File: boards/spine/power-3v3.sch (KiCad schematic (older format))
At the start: 14 parts, among them U9 RT8299A

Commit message: BOM tweaks, starting DC/DC fixes
VCC is not active until EN goes high, so EN must be
connected to VIN via the 100k resistor. Internal resistance
is 5k to a 3V zener.
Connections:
- net +5V: now also R25.1
- net at C57.1, U9.8 (VCC): no longer R25.1
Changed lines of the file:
@@
 	4250 4300 4150 4300
-Wire Wire Line
-	4150 4300 4150 4050
-Connection ~ 4150 4050
 Wire Wire Line
 	6250 3800 6500 3800
@@
 Text Notes 3750 5100 0    60   ~ 0
 High efficiency DC-DC converter, 3.3V at 3A
+Wire Wire Line
+	4150 4300 4150 3800
+Connection ~ 4150 3800
 $EndSCHEMATC

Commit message: BOM cleanup
Especially fix the confusing and mostly incorrect Mfg/Mfr stuff that I inherited from somewhere.
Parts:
- C55, C56, C60, C61: Mfg1 (none) -> Murata; Mfg1Id (none) -> GRM31CR61H106MA12L; MfgId GRM31CR61H106MA12L -> (none); MfrId Murata -> (none)
- C57: Mfg1 (none) -> Murata; Mfg1Id (none) -> GRM219R61H105KA73D; MfgId GRM219R61H105KA73D -> (none); MfrId Murata -> (none)
- C58: Mfg1 (none) -> Murata; Mfg1Id (none) -> GRM21BR71H104MA01L; MfgId GRM21BR71H104MA01L -> (none); MfrId Murata -> (none)
- C59: Mfg1 (none) -> Murata; Mfg1Id (none) -> GRM2165C1H101JA01D; MfgId GRM2165C1H101JA01D -> (none); MfrId Murata -> (none)
- D6: Mfg1 (none) -> Diodes Inc; Mfg1Id (none) -> BAT54C-7-F; MfgId BAT54C-7-F -> (none); MfrId Diodes Inc -> (none)
- L2: Mfg1 (none) -> Bourns; Mfg1Id (none) -> SRR1280-220M; MfgId Bourns -> (none); MfrId SRR1280-220M -> (none)
- R25: Mfg1 (none) -> Stackpole; Mfg1Id (none) -> RMCF0805JT100K; MfgId RMCF0805JT100K -> (none); MfrId Stackpole -> (none)
- R26: Mfg1 (none) -> Stackpole; Mfg1Id (none) -> RMCF0805JT150R; MfgId RMCF0805JT150R -> (none); MfrId Stackpole -> (none)
- R27: Mfg1 (none) -> Stackpole; Mfg1Id (none) -> RMCF0805FT16K0; MfgId RMCF0805FT16K0 -> (none); MfrId Stackpole -> (none)
- R28: Mfg1 (none) -> Stackpole; Mfg1Id (none) -> RMCF0805FT5K10; MfgId RMCF0805FT5K10 -> (none); MfrId Stackpole -> (none)
- U9: Mfg1 (none) -> Richtek; Mfg1Id (none) -> RT8299AZSP; MfgId RT8299AZSP -> (none); MfrId Richtek -> (none)
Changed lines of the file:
@@
 F 3 "https://www.seielect.com/Catalog/SEI-RMCF_RMCP.pdf" H 4400 4300 30  0001 C CNN
 F 4 "Digikey" V 4400 4300 60  0001 C CNN "Vend1"
-F 5 "Stackpole" V 4400 4300 60  0001 C CNN "MfrId"
-F 6 "RMCF0805JT100K" V 4400 4300 60  0001 C CNN "MfgId"
+F 5 "Stackpole" V 4400 4300 60  0001 C CNN "Mfg1"
+F 6 "RMCF0805JT100K" V 4400 4300 60  0001 C CNN "Mfg1Id"
 F 7 "RMCF0805JT100KCT-ND" V 4400 4300 60  0001 C CNN "Vend1Id"
 F 8 "0.00320" V 4400 4300 60  0001 C CNN "RefPrice1k"
@@
 F 2 "Capacitors_SMD:C_1206" H 3338 4050 30  0001 C CNN
 F 3 "http://www.murata.com/~/media/webrenewal/support/library/catalog/products/capacitor/mlcc/c02e.ashx" H 3300 4200 60  0001 C CNN
-F 4 "GRM31CR61H106MA12L" H 3350 4000 39  0001 L BNN "MfgId"
-F 5 "Murata" H 3300 4200 60  0001 C CNN "MfrId"
+F 4 "GRM31CR61H106MA12L" H 3350 4000 39  0001 L BNN "Mfg1Id"
+F 5 "Murata" H 3300 4200 60  0001 C CNN "Mfg1"
 F 6 "Digikey" H 3300 4200 60  0001 C CNN "Vend1"
 F 7 "490-10756-2-ND" H 3300 4200 60  0001 C CNN "Vend1Id"
@@
 F 2 "Capacitors_SMD:C_0805" H 3888 4200 30  0001 C CNN
 F 3 "http://www.murata.com/~/media/webrenewal/support/library/catalog/products/capacitor/mlcc/c02e.ashx" H 3850 4350 60  0001 C CNN
-F 4 "GRM219R61H105KA73D" H 3900 4150 39  0001 L BNN "MfgId"
-F 5 "Murata" H 3850 4350 60  0001 C CNN "MfrId"
+F 4 "GRM219R61H105KA73D" H 3900 4150 39  0001 L BNN "Mfg1Id"
+F 5 "Murata" H 3850 4350 60  0001 C CNN "Mfg1"
 F 6 "Digikey" H 3850 4350 60  0001 C CNN "Vend1"
 F 7 "490-10743-2-ND" H 3850 4350 60  0001 C CNN "Vend1Id"
@@
 F 4 "Digikey" H 5050 3600 60  0001 C CNN "Vend1"
 F 5 "1028-1295-1-ND" H 5050 3600 60  0001 C CNN "Vend1Id"
-F 6 "Richtek" H 5050 3600 60  0001 C CNN "MfrId"
-F 7 "RT8299AZSP" H 5050 3600 60  0001 C CNN "MfgId"
+F 6 "Richtek" H 5050 3600 60  0001 C CNN "Mfg1"
+F 7 "RT8299AZSP" H 5050 3600 60  0001 C CNN "Mfg1Id"
 F 8 "0.37752" H 5050 3600 60  0001 C CNN "RefPrice1k"
 	1    5050 3600
@@
 F 5 "490-9672-2-ND" V 6100 3800 60  0001 C CNN "Vend1Id"
 F 6 "Digikey" V 6100 3800 60  0001 C CNN "Vend1"
-F 7 "Murata" V 6100 3800 60  0001 C CNN "MfrId"
-F 8 "GRM21BR71H104MA01L" V 6100 3800 60  0001 C CNN "MfgId"
+F 7 "Murata" V 6100 3800 60  0001 C CNN "Mfg1"
+F 8 "GRM21BR71H104MA01L" V 6100 3800 60  0001 C CNN "Mfg1Id"
 	1    6100 3800
 	0    1    1    0
@@
 F 3 "http://www.bourns.com/docs/Product-Datasheets/SRR1280.pdf" H 6500 3400 60  0001 C CNN
 F 4 "SRR1280-220MTR-ND" V 6500 3400 60  0001 C CNN "Vend1Id"
-F 5 "Bourns" V 6500 3400 60  0001 C CNN "MfgId"
-F 6 "SRR1280-220M" V 6500 3400 60  0001 C CNN "MfrId"
+F 5 "Bourns" V 6500 3400 60  0001 C CNN "Mfg1"
+F 6 "SRR1280-220M" V 6500 3400 60  0001 C CNN "Mfg1Id"
 F 7 "Digikey" V 6500 3400 60  0001 C CNN "Vend1"
 F 8 "0.42160" V 6500 3400 60  0001 C CNN "RefPrice1k"
@@
 F 5 "RMCF0805JT150RCT-ND" V 6500 4600 60  0001 C CNN "Vend1Id"
 F 6 "Digikey" V 6500 4600 60  0001 C CNN "Vend1"
-F 7 "Stackpole" V 6500 4600 60  0001 C CNN "MfrId"
-F 8 "RMCF0805JT150R" V 6500 4600 60  0001 C CNN "MfgId"
+F 7 "Stackpole" V 6500 4600 60  0001 C CNN "Mfg1"
+F 8 "RMCF0805JT150R" V 6500 4600 60  0001 C CNN "Mfg1Id"
 	1    6500 4600
 	-1   0    0    1
@@
 F 5 "490-1615-1-ND" V 6500 4900 60  0001 C CNN "Vend1Id"
 F 6 "Digikey" V 6500 4900 60  0001 C CNN "Vend1"
-F 7 "Murata" V 6500 4900 60  0001 C CNN "MfrId"
-F 8 "GRM2165C1H101JA01D" V 6500 4900 60  0001 C CNN "MfgId"
+F 7 "Murata" V 6500 4900 60  0001 C CNN "Mfg1"
+F 8 "GRM2165C1H101JA01D" V 6500 4900 60  0001 C CNN "Mfg1Id"
 	1    6500 4900
 	-1   0    0    1
@@
 F 2 "Capacitors_SMD:C_1206" H 3588 4050 30  0001 C CNN
 F 3 "http://www.murata.com/~/media/webrenewal/support/library/catalog/products/capacitor/mlcc/c02e.ashx" H 3550 4200 60  0001 C CNN
-F 4 "GRM31CR61H106MA12L" H 3600 4000 39  0001 L BNN "MfgId"
-F 5 "Murata" H 3550 4200 60  0001 C CNN "MfrId"
+F 4 "GRM31CR61H106MA12L" H 3600 4000 39  0001 L BNN "Mfg1Id"
+F 5 "Murata" H 3550 4200 60  0001 C CNN "Mfg1"
 F 6 "Digikey" H 3550 4200 60  0001 C CNN "Vend1"
 F 7 "490-10756-2-ND" H 3550 4200 60  0001 C CNN "Vend1Id"
@@
 F 2 "Capacitors_SMD:C_1206" H 7638 4050 30  0001 C CNN
 F 3 "http://www.murata.com/~/media/webrenewal/support/library/catalog/products/capacitor/mlcc/c02e.ashx" H 7600 4200 60  0001 C CNN
-F 4 "GRM31CR61H106MA12L" H 7650 4000 39  0001 L BNN "MfgId"
-F 5 "Murata" H 7600 4200 60  0001 C CNN "MfrId"
+F 4 "GRM31CR61H106MA12L" H 7650 4000 39  0001 L BNN "Mfg1Id"
+F 5 "Murata" H 7600 4200 60  0001 C CNN "Mfg1"
 F 6 "Digikey" H 7600 4200 60  0001 C CNN "Vend1"
 F 7 "490-10756-2-ND" H 7600 4200 60  0001 C CNN "Vend1Id"
@@
 F 2 "Capacitors_SMD:C_1206" H 7888 4050 30  0001 C CNN
 F 3 "http://www.murata.com/~/media/webrenewal/support/library/catalog/products/capacitor/mlcc/c02e.ashx" H 7850 4200 60  0001 C CNN
-F 4 "GRM31CR61H106MA12L" H 7900 4000 39  0001 L BNN "MfgId"
-F 5 "Murata" H 7850 4200 60  0001 C CNN "MfrId"
+F 4 "GRM31CR61H106MA12L" H 7900 4000 39  0001 L BNN "Mfg1Id"
+F 5 "Murata" H 7850 4200 60  0001 C CNN "Mfg1"
 F 6 "Digikey" H 7850 4200 60  0001 C CNN "Vend1"
 F 7 "490-10756-2-ND" H 7850 4200 60  0001 C CNN "Vend1Id"
@@
 F 3 "https://www.seielect.com/Catalog/SEI-RMCF_RMCP.pdf" H 7150 4600 30  0001 C CNN
 F 4 "Digikey" V 7150 4600 60  0001 C CNN "Vend1"
-F 5 "Stackpole" V 7150 4600 60  0001 C CNN "MfrId"
-F 6 "RMCF0805FT5K10" V 7150 4600 60  0001 C CNN "MfgId"
+F 5 "Stackpole" V 7150 4600 60  0001 C CNN "Mfg1"
+F 6 "RMCF0805FT5K10" V 7150 4600 60  0001 C CNN "Mfg1Id"
 F 7 "RMCF0805FT5K10CT-ND" V 7150 4600 60  0001 C CNN "Vend1Id"
 F 8 "0.00448" V 7150 4600 60  0001 C CNN "RefPrice1k"
@@
 F 3 "https://www.seielect.com/Catalog/SEI-RMCF_RMCP.pdf" H 7150 4000 30  0001 C CNN
 F 4 "Digikey" V 7150 4000 60  0001 C CNN "Vend1"
-F 5 "Stackpole" V 7150 4000 60  0001 C CNN "MfrId"
-F 6 "RMCF0805FT16K0" V 7150 4000 60  0001 C CNN "MfgId"
+F 5 "Stackpole" V 7150 4000 60  0001 C CNN "Mfg1"
+F 6 "RMCF0805FT16K0" V 7150 4000 60  0001 C CNN "Mfg1Id"
 F 7 "RMCF0805FT16K0CT-ND" V 7150 4000 60  0001 C CNN "Vend1Id"
 F 8 "0.00448" V 7150 4000 60  0001 C CNN "RefPrice1k"
@@
 F 2 "TO_SOT_Packages_SMD:SOT-23" H 5750 3000 60  0001 C CNN
 F 3 "http://www.diodes.com/_files/datasheets/ds11005.pdf" H 5750 3000 60  0001 C CNN
-F 4 "Diodes Inc" H 5750 3150 39  0001 C CNN "MfrId"
-F 5 "BAT54C-7-F" H 5750 3100 39  0000 C CNN "MfgId"
+F 4 "Diodes Inc" H 5750 3150 39  0001 C CNN "Mfg1"
+F 5 "BAT54C-7-F" H 5750 3100 39  0000 C CNN "Mfg1Id"
 F 6 "BAT54C-FDICT-ND" V 5750 3000 60  0001 C CNN "Vend1Id"
 F 7 ".03955" V 5750 3000 60  0001 C CNN "RefPrice1k"
@@
 FB 59 00 E6 A5 69 3A 37 9E CF 73 BC F7 37 E3 33 5D 9E A8 3E 7F 80 FA F7 F6 BB 44 F4 6E D4 E7 77
 A2 1E 1F 27 A2 E3 16 70 32 E9 54 FE 3F E7 AF 00 CA 1C A3 36 0A 00 00 00 00 49 45 4E 44 AE 42 60
-82 00
+82 70
 EndData
 $EndBitmap

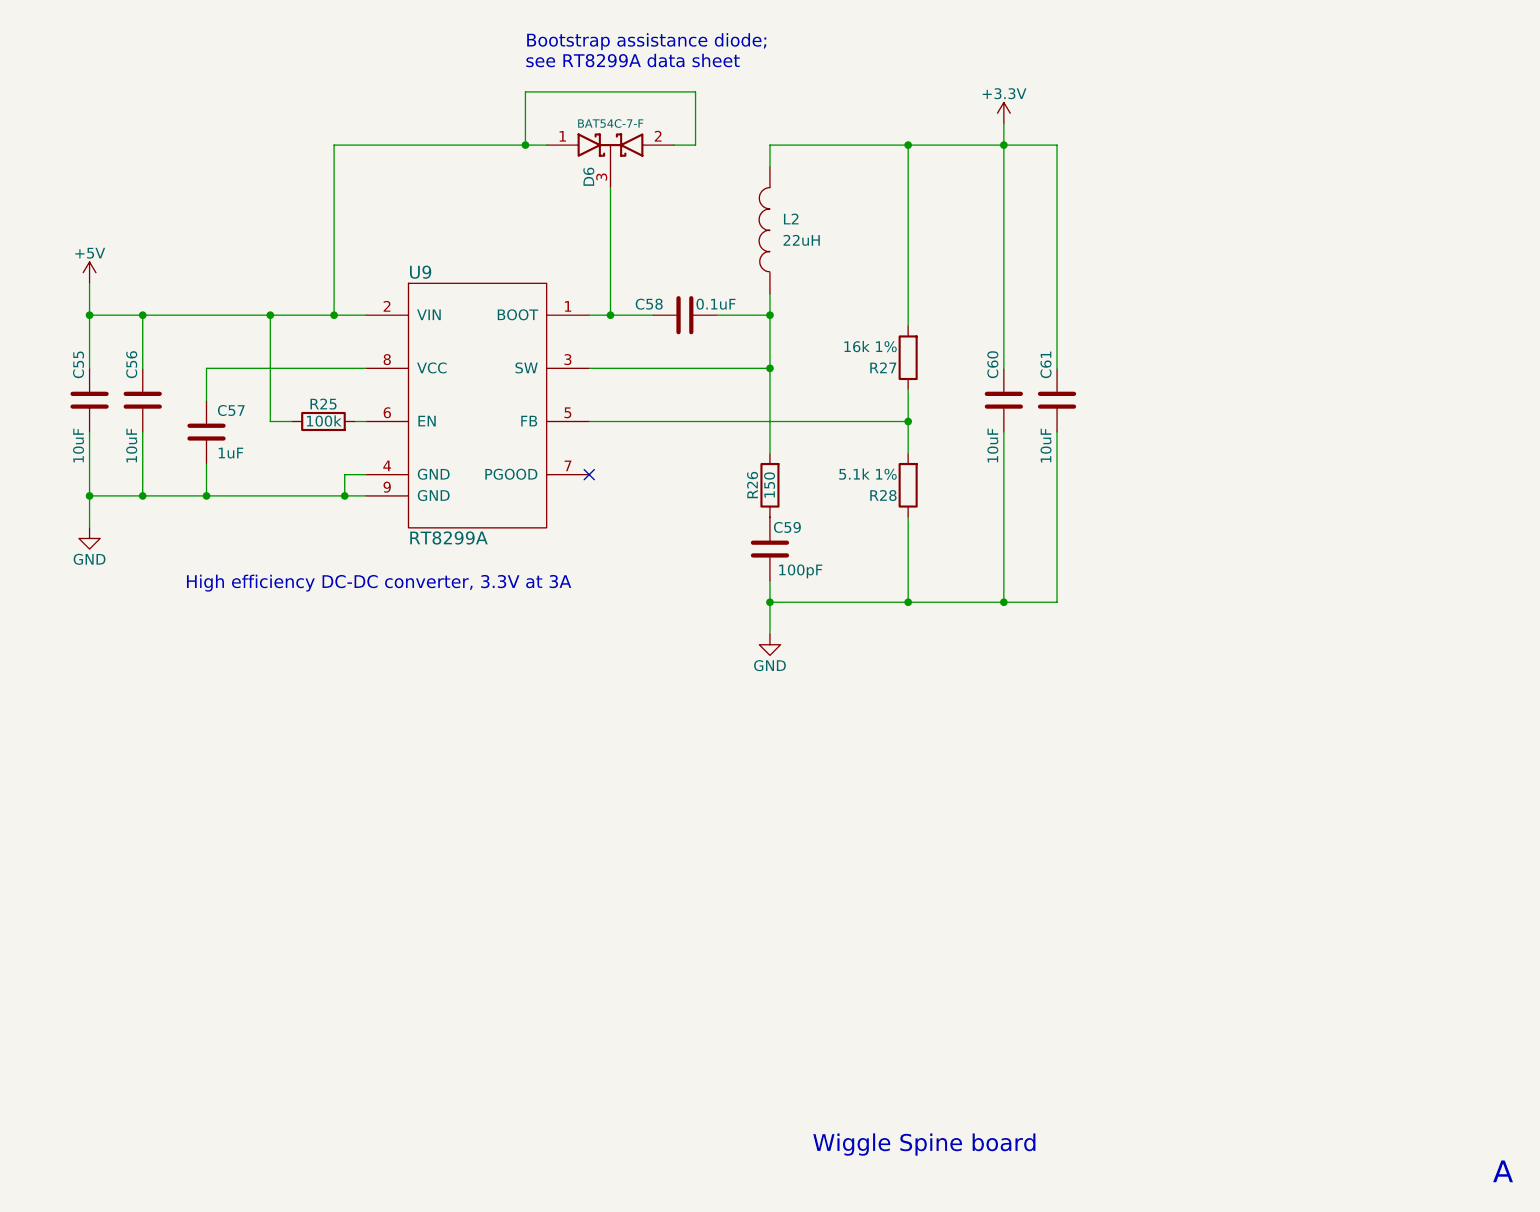
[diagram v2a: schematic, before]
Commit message: Capacitor upgrades, BOM tidying
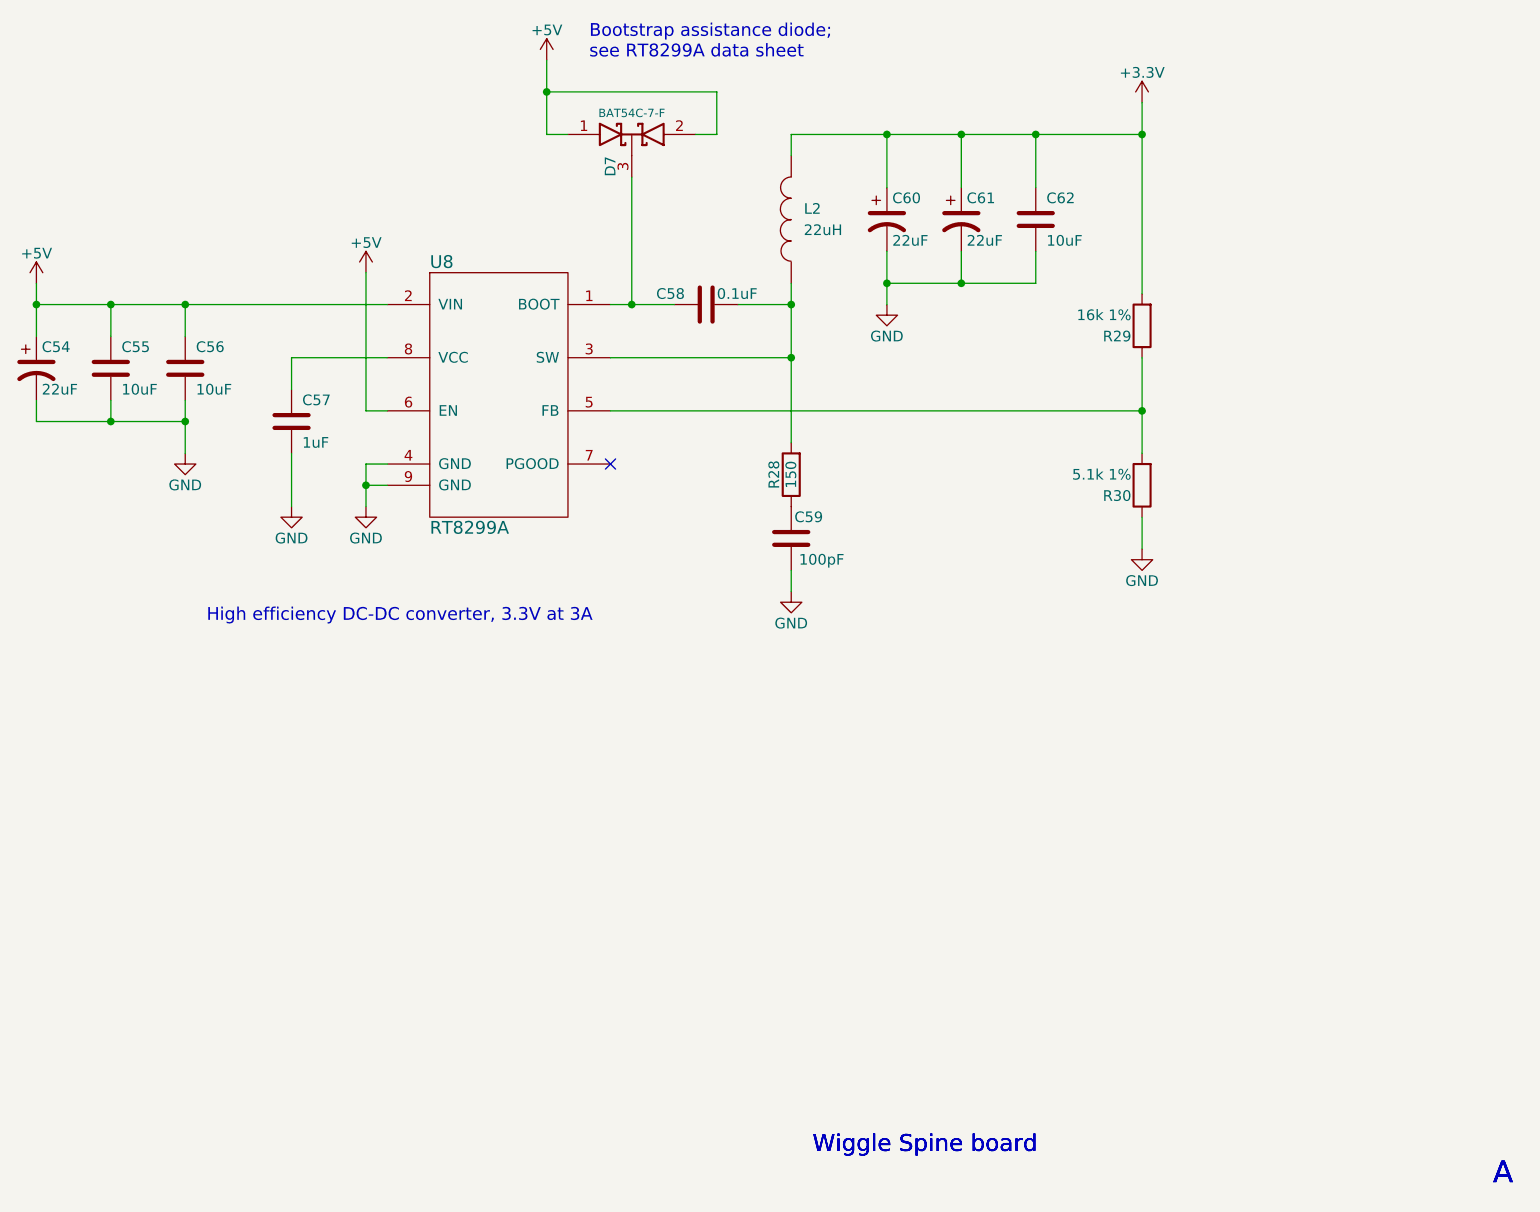
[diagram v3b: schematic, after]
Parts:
- removed C60, C61: 10uF, Capacitors_SMD:C_1206, symbol C
- removed R25: 100k, Resistors_SMD:R_0805, symbol R
- added C54, C60, C61: 22uF, Capacitors_SMD:c_elec_6.3x7.7, symbol CP1
- added C62: 10uF, Capacitors_SMD:C_1206, symbol C
- renumbered D6 to D7, R26 to R28, R27 to R29, R28 to R30, U9 to U8
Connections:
- net +3V3: now also C60.1, C61.1, C62.1
- net +5V: now also U8.6 (EN), C54.1
- net GND: now also C54.2, C60.2, C61.2, C62.2
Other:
- moved on the sheet: C57, C58, C59, D7, L2, R28, R29, R30, U8

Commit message: About 50% dimmer blue LED when FPGA is unconfigured
This seems a good compromise between visibility while debugging and unobtrusiveness during normal operation.
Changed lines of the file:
@@
 $EndComp
 Wire Wire Line
-	5750 3750 5850 3750
-Wire Wire Line
-	5850 3750 6050 3750
+	5750 3750 6050 3750
 Wire Wire Line
 	4700 4500 4600 4500
 Wire Wire Line
-	4600 4500 4600 4600
-Wire Wire Line
-	4600 4600 4600 4700
+	4600 4500 4600 4700
 Wire Wire Line
 	4600 4600 4700 4600
@@
 	6350 3750 6600 3750
 Wire Wire Line
-	6600 3650 6600 3750
-Wire Wire Line
-	6600 3750 6600 4000
-Wire Wire Line
-	6600 4000 6600 4400
+	6600 3650 6600 4400
 $Comp
 L R R30
@@
 	5750 4250 8250 4250
 Wire Wire Line
-	8250 4000 8250 4250
-Wire Wire Line
-	8250 4250 8250 4450
+	8250 4000 8250 4450
 Connection ~ 8250 4250
 Wire Wire Line
 	6600 3050 6600 2950
 Wire Wire Line
-	8250 2800 8250 2950
-Wire Wire Line
-	8250 2950 8250 3700
+	8250 2800 8250 3700
 Connection ~ 8250 2950
 $Comp
-L GND #PWR138
+L GND #PWR0132
 U 1 1 564CF3C3
 P 6600 5100
-F 0 "#PWR138" H 6600 4850 50  0001 C CNN
+F 0 "#PWR0132" H 6600 4850 50  0001 C CNN
 F 1 "GND" H 6600 4950 50  0000 C CNN
 F 2 "" H 6600 5100 60  0000 C CNN
@@
 NoConn ~ 5750 4500
 $Comp
-L +5V #PWR132
+L +5V #PWR0133
 U 1 1 564CF485
 P 3050 3650
-F 0 "#PWR132" H 3050 3500 50  0001 C CNN
+F 0 "#PWR0133" H 3050 3500 50  0001 C CNN
 F 1 "+5V" H 3050 3790 50  0000 C CNN
 F 2 "" H 3050 3650 60  0000 C CNN
@@
 $EndComp
 $Comp
-L +3.3V #PWR140
+L +3.3V #PWR0134
 U 1 1 564CF4B3
 P 8250 2800
-F 0 "#PWR140" H 8250 2650 50  0001 C CNN
+F 0 "#PWR0134" H 8250 2650 50  0001 C CNN
 F 1 "+3.3V" H 8250 2940 50  0000 C CNN
 F 2 "" H 8250 2800 60  0000 C CNN
@@
 $EndComp
 Wire Wire Line
-	6600 2950 7050 2950
-Wire Wire Line
-	7050 2950 7400 2950
-Wire Wire Line
-	7400 2950 7750 2950
-Wire Wire Line
-	7750 2950 8250 2950
+	6600 2950 8250 2950
 $Comp
 L D_Schottky_x2_KCom_AAK D7
@@
 72 0F 1C A9 DC 70 49 CB 79 33 88 85 99 AD 01 6C 4B 10 FC 3B 13 DE 3B 37 68 79 AD 07 BC 00 3C 0E
 3C 31 EE E3 D8 E7 0F 03 D7 7B 9F FB C1 E1 FF 01 18 C4 96 1D B8 0E 40 07 00 00 00 00 49 45 4E 44
-AE 42 60 82 10
+AE 42 60 82 00
 EndData
 $EndBitmap
@@
 FB 59 00 E6 A5 69 3A 37 9E CF 73 BC F7 37 E3 33 5D 9E A8 3E 7F 80 FA F7 F6 BB 44 F4 6E D4 E7 77
 A2 1E 1F 27 A2 E3 16 70 32 E9 54 FE 3F E7 AF 00 CA 1C A3 36 0A 00 00 00 00 49 45 4E 44 AE 42 60
-82 00
+82 70
 EndData
 $EndBitmap
@@
 72 0F 1C A9 DC 70 49 CB 79 33 88 85 99 AD 01 6C 4B 10 FC 3B 13 DE 3B 37 68 79 AD 07 BC 00 3C 0E
 3C 31 EE E3 D8 E7 0F 03 D7 7B 9F FB C1 E1 FF 01 18 C4 96 1D B8 0E 40 07 00 00 00 00 49 45 4E 44
-AE 42 60 82 00
+AE 42 60 82 4D
 EndData
 $EndBitmap
@@
 	3750 3750 3750 3900
 Wire Wire Line
-	3050 3750 3400 3750
-Wire Wire Line
-	3400 3750 3750 3750
-Wire Wire Line
-	3750 3750 4700 3750
+	3050 3750 4700 3750
 $Comp
 L CP1 C54
@@
 $EndComp
 $Comp
-L GND #PWR133
+L GND #PWR0135
 U 1 1 567A52BC
 P 3750 4450
-F 0 "#PWR133" H 3750 4200 50  0001 C CNN
+F 0 "#PWR0135" H 3750 4200 50  0001 C CNN
 F 1 "GND" H 3750 4300 50  0000 C CNN
 F 2 "" H 3750 4450 60  0000 C CNN
@@
 $EndComp
 Wire Wire Line
-	3750 4200 3750 4300
-Wire Wire Line
-	3750 4300 3750 4450
+	3750 4200 3750 4450
 $Comp
 L C C55
@@
 $EndComp
 Wire Wire Line
-	3050 4300 3400 4300
-Wire Wire Line
-	3400 4300 3750 4300
+	3050 4300 3750 4300
 Wire Wire Line
 	3400 4300 3400 4200
@@
 	3400 3750 3400 3900
 Wire Wire Line
-	3050 3750 3050 3900
+	3050 3650 3050 3900
 Connection ~ 3400 3750
-Wire Wire Line
-	3050 3650 3050 3750
 Connection ~ 3050 3750
 $Comp
-L +5V #PWR137
+L +5V #PWR0136
 U 1 1 567A5ADD
 P 5450 2600
-F 0 "#PWR137" H 5450 2450 50  0001 C CNN
+F 0 "#PWR0136" H 5450 2450 50  0001 C CNN
 F 1 "+5V" H 5450 2740 50  0000 C CNN
 F 2 "" H 5450 2600 60  0000 C CNN
@@
 $EndComp
 Wire Wire Line
-	5450 2600 5450 2750
-Wire Wire Line
-	5450 2750 5450 2950
+	5450 2600 5450 2950
 Wire Wire Line
 	5450 2950 5550 2950
 Connection ~ 5450 2750
 $Comp
-L +5V #PWR135
+L +5V #PWR0137
 U 1 1 567A5C43
 P 4600 3600
-F 0 "#PWR135" H 4600 3450 50  0001 C CNN
+F 0 "#PWR0137" H 4600 3450 50  0001 C CNN
 F 1 "+5V" H 4600 3740 50  0000 C CNN
 F 2 "" H 4600 3600 60  0000 C CNN
@@
 	6600 5000 6600 5100
 $Comp
-L GND #PWR141
+L GND #PWR0138
 U 1 1 567A60B0
 P 8250 4900
-F 0 "#PWR141" H 8250 4650 50  0001 C CNN
+F 0 "#PWR0138" H 8250 4650 50  0001 C CNN
 F 1 "GND" H 8250 4750 50  0000 C CNN
 F 2 "" H 8250 4900 60  0000 C CNN
@@
 Connection ~ 7750 2950
 $Comp
-L GND #PWR139
+L GND #PWR0139
 U 1 1 567A68F4
 P 7050 3750
-F 0 "#PWR139" H 7050 3500 50  0001 C CNN
+F 0 "#PWR0139" H 7050 3500 50  0001 C CNN
 F 1 "GND" H 7050 3600 50  0000 C CNN
 F 2 "" H 7050 3750 60  0000 C CNN
@@
 $EndComp
 Wire Wire Line
-	7050 3500 7050 3650
-Wire Wire Line
-	7050 3650 7050 3750
+	7050 3500 7050 3750
 Wire Wire Line
 	7400 3500 7400 3650
 Wire Wire Line
-	7050 3650 7400 3650
-Wire Wire Line
-	7400 3650 7750 3650
+	7050 3650 7750 3650
 Connection ~ 7050 3650
 Wire Wire Line
@@
 Connection ~ 7400 3650
 $Comp
-L GND #PWR136
+L GND #PWR0140
 U 1 1 567A6DAA
 P 4600 4700
-F 0 "#PWR136" H 4600 4450 50  0001 C CNN
+F 0 "#PWR0140" H 4600 4450 50  0001 C CNN
 F 1 "GND" H 4600 4550 50  0000 C CNN
 F 2 "" H 4600 4700 60  0000 C CNN
@@
 $EndComp
 $Comp
-L GND #PWR134
+L GND #PWR0141
 U 1 1 567A6DF1
 P 4250 4700
-F 0 "#PWR134" H 4250 4450 50  0001 C CNN
+F 0 "#PWR0141" H 4250 4450 50  0001 C CNN
 F 1 "GND" H 4250 4550 50  0000 C CNN
 F 2 "" H 4250 4700 60  0000 C CNN
